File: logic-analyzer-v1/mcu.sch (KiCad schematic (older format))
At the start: 18 parts

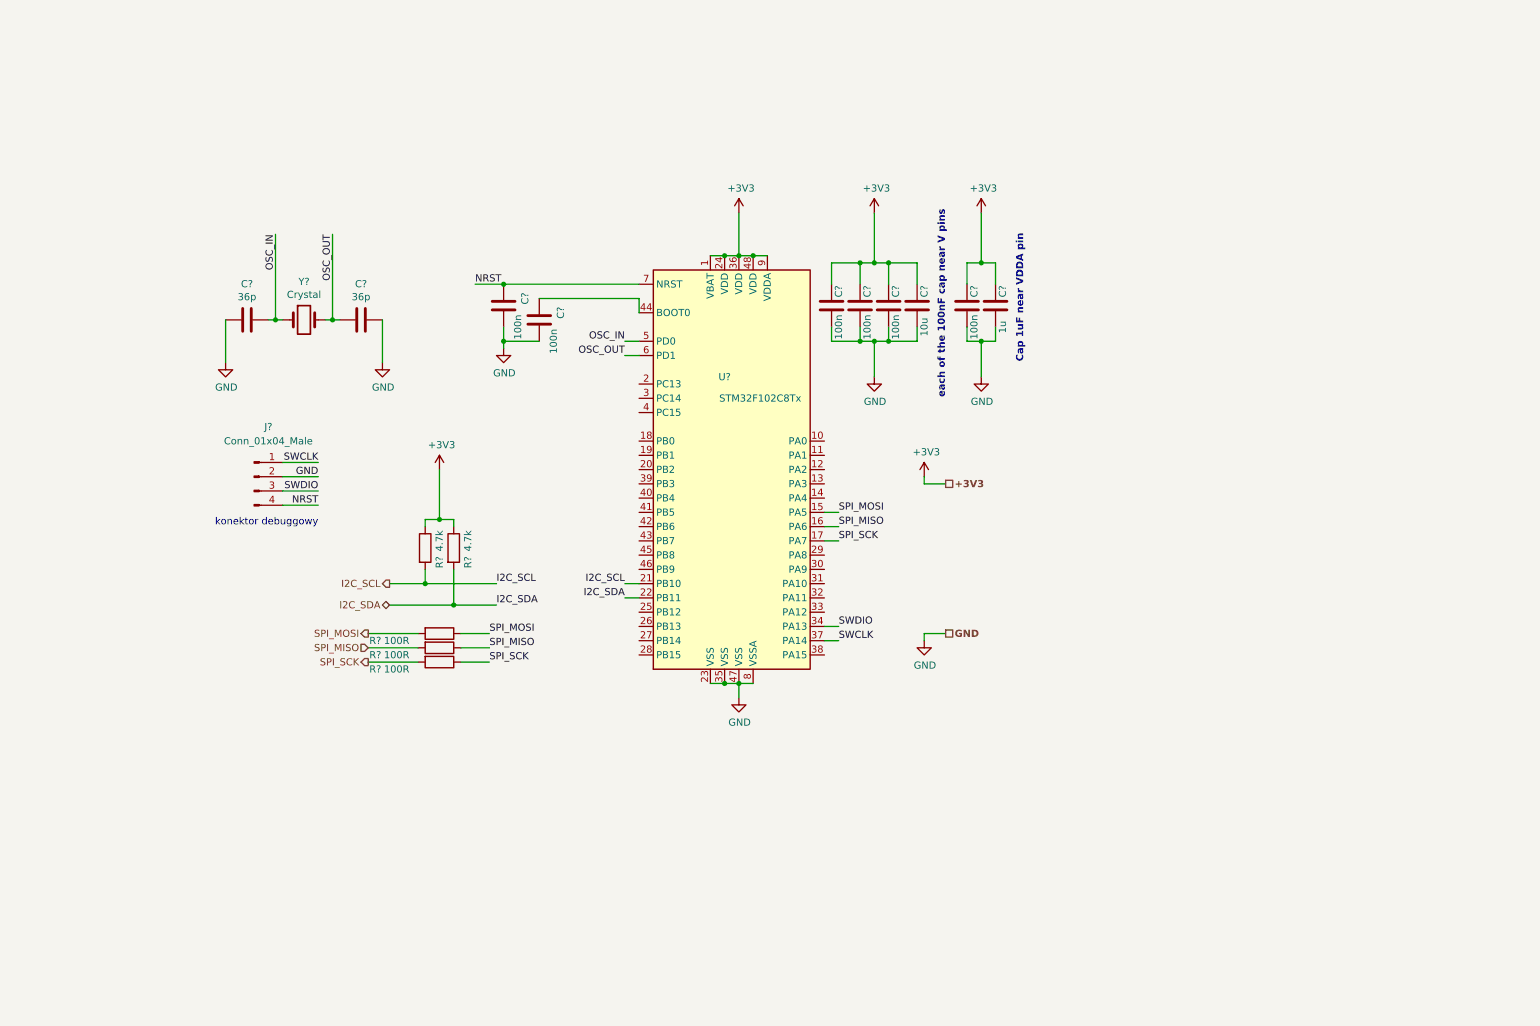
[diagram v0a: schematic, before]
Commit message: MOD usb power nets fix, mcu fixes
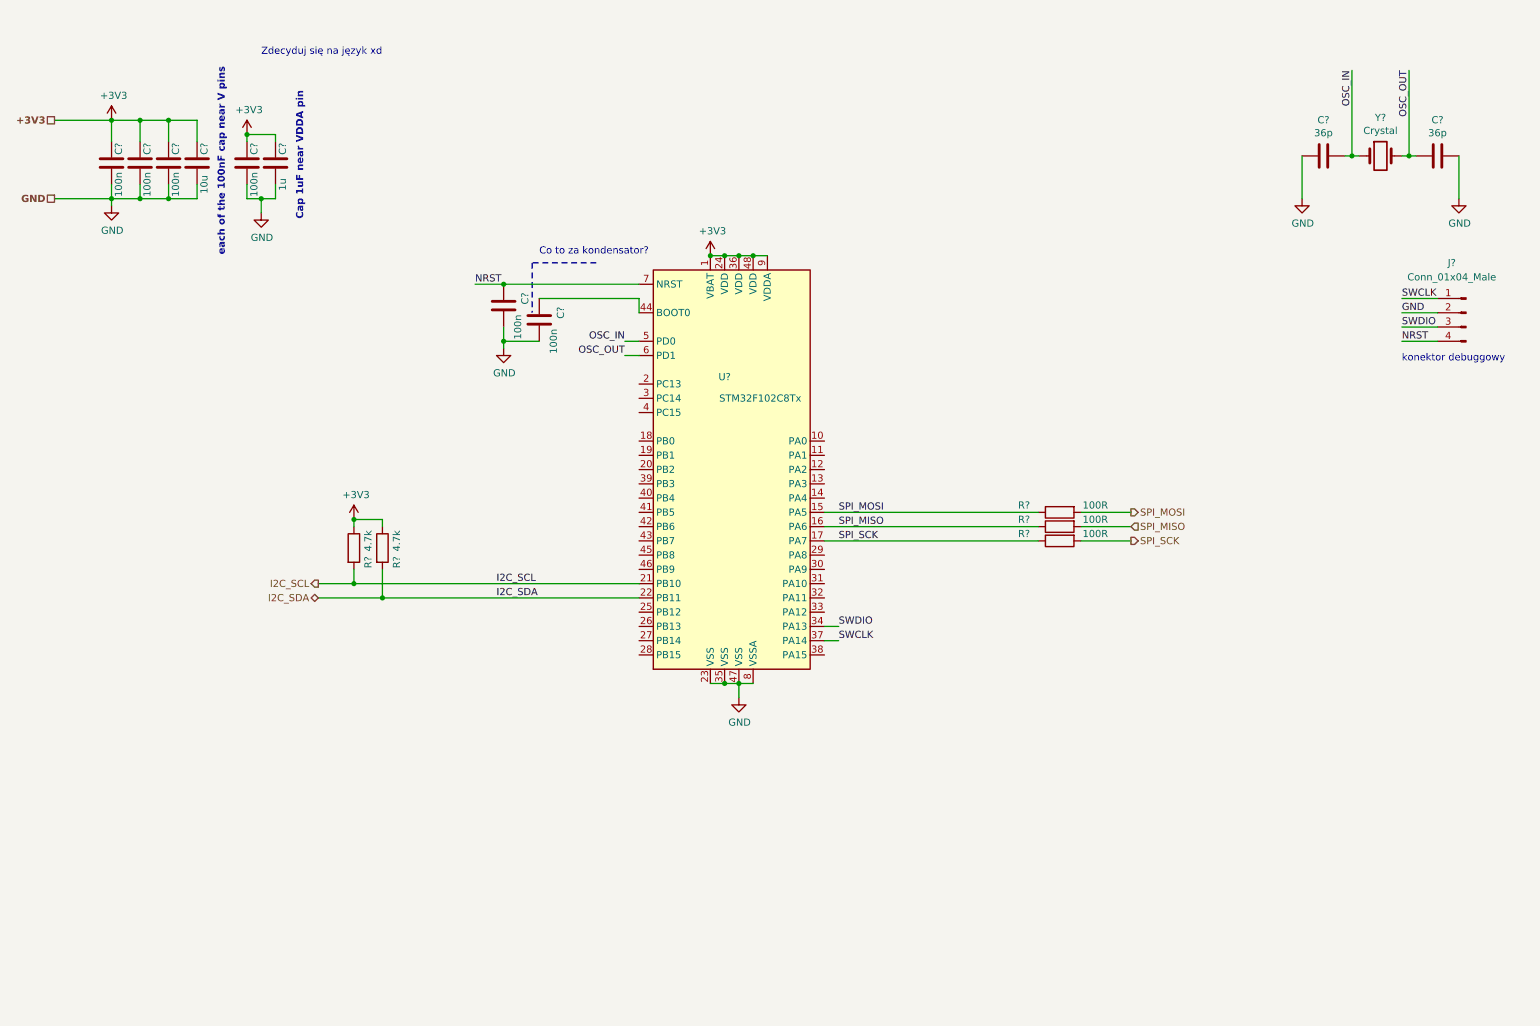
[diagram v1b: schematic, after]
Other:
- note added: "Co to za kondensator?\n"
- note added: "Zdecyduj się na język xd"
- moved on the sheet: C?, J?, R?, Y?

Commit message: adding gpio pins, usb pins, usart pins
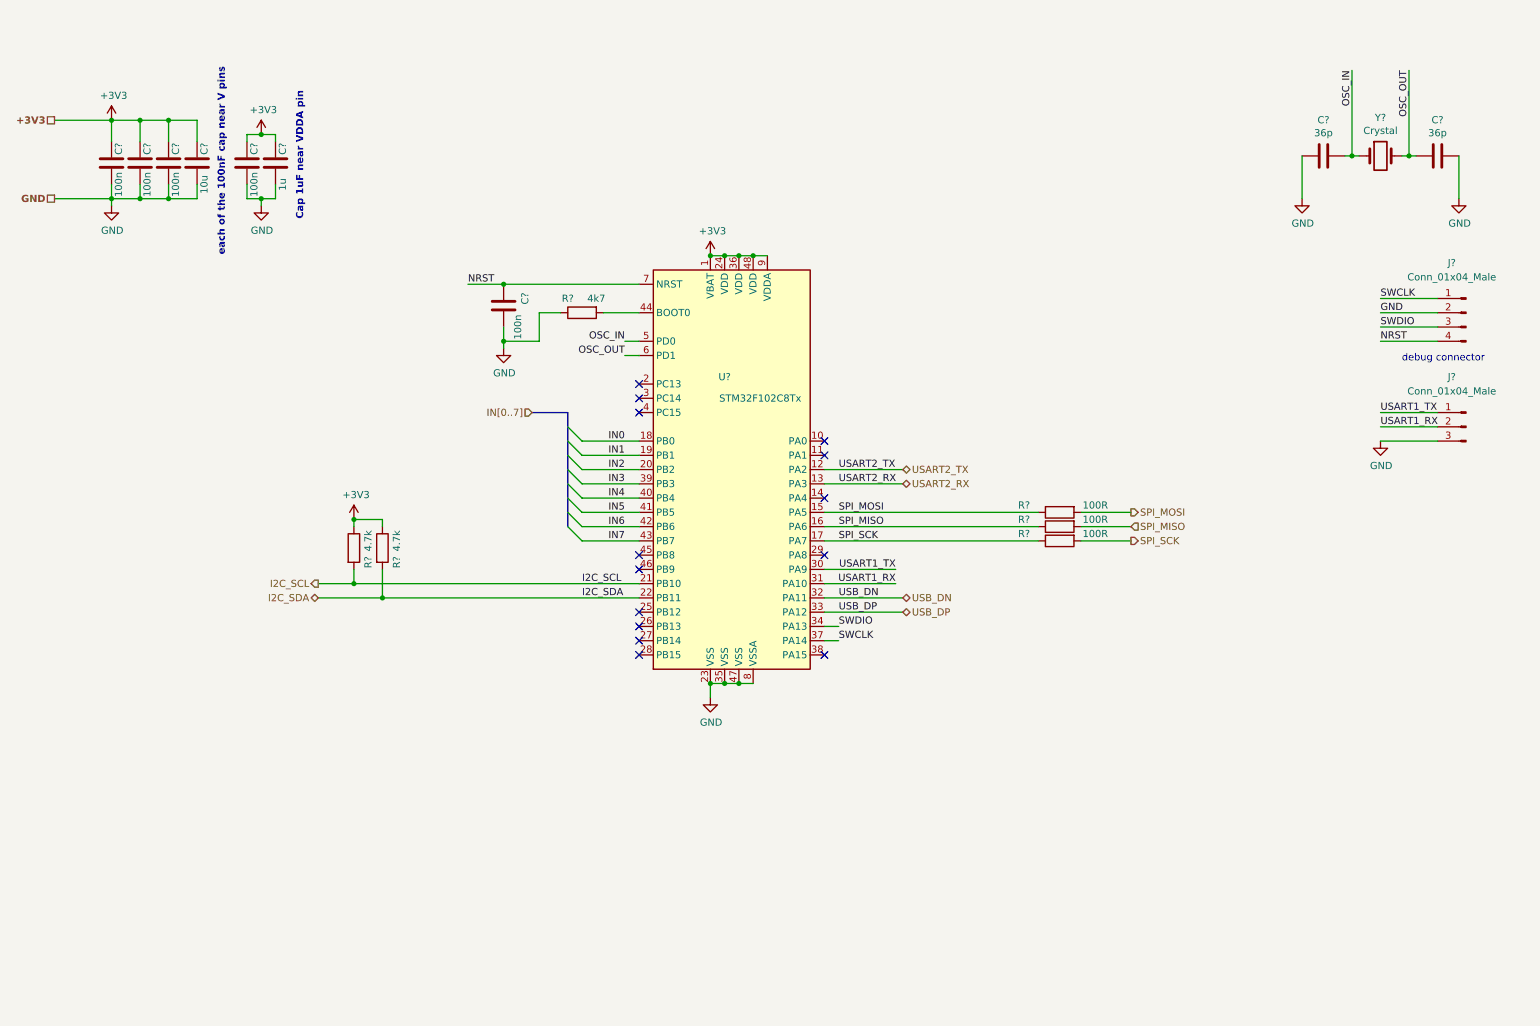
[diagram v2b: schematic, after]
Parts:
- removed C?: 100n, Capacitor_SMD:C_0603_1608Metric_Pad1.05x0.95mm_HandSolder, symbol Device:C
- added J?: Conn_01x04_Male, symbol Connector:Conn_01x03_Male
- added R?: 4k7, Resistor_SMD:R_0603_1608Metric_Pad1.05x0.95mm_HandSolder, symbol Device:R
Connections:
- net GND: now also J?.3 (Pin_3), R?.1
- net USART2_TX: now reaches U?.12 (PA2)
- net USART2_RX: now reaches U?.13 (PA3)
- net IN0: now reaches U?.18 (PB0)
- net IN1: now reaches U?.19 (PB1)
- net IN2: now reaches U?.20 (PB2)
- net USART1_TX: now reaches U?.30 (PA9)
- net USART1_TX: now also J?.1 (Pin_1)
- net USART1_RX: now reaches U?.31 (PA10)
- net USART1_RX: now also J?.2 (Pin_2)
- net USB_DN: now reaches U?.32 (PA11)
- net USB_DP: now reaches U?.33 (PA12)
- net IN3: now reaches U?.39 (PB3)
- net IN4: now reaches U?.40 (PB4)
- net IN5: now reaches U?.41 (PB5)
- net IN6: now reaches U?.42 (PB6)
- net IN7: now reaches U?.43 (PB7)
- net at U?.44 (BOOT0): now also R?.2
- no-connect marks 0 -> 14
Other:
- note added: "debug connector"
- note removed: "Co to za kondensator?\n"
- note removed: "Zdecyduj się na język xd"
- note removed: "konektor debuggowy"
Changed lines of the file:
@@
 L power:GND #PWR?
 U 1 1 5F3DC23A
-P 2250 2000
-F 0 "#PWR?" H 2250 1750 50  0001 C CNN
-F 1 "GND" H 2255 1827 50  0000 C CNN
-F 2 "" H 2250 2000 50  0001 C CNN
-F 3 "" H 2250 2000 50  0001 C CNN
-	1    2250 2000
-	1    0    0    -1
-$EndComp
-Wire Wire Line
-	2250 2000 2250 1900
+P 2250 1950
+F 0 "#PWR?" H 2250 1700 50  0001 C CNN
+F 1 "GND" H 2255 1777 50  0000 C CNN
+F 2 "" H 2250 1950 50  0001 C CNN
+F 3 "" H 2250 1950 50  0001 C CNN
+	1    2250 1950
+	1    0    0    -1
+$EndComp
+Wire Wire Line
+	2250 1950 2250 1900
 $Comp
 L power:GND #PWR?
 U 1 1 5F3DDEC8
-P 5600 5400
-F 0 "#PWR?" H 5600 5150 50  0001 C CNN
-F 1 "GND" H 5605 5227 50  0000 C CNN
-F 2 "" H 5600 5400 50  0001 C CNN
-F 3 "" H 5600 5400 50  0001 C CNN
-	1    5600 5400
-	1    0    0    -1
-$EndComp
-Wire Wire Line
-	5600 5400 5600 5300
+P 5400 5400
+F 0 "#PWR?" H 5400 5150 50  0001 C CNN
+F 1 "GND" H 5405 5227 50  0000 C CNN
+F 2 "" H 5400 5400 50  0001 C CNN
+F 3 "" H 5400 5400 50  0001 C CNN
+	1    5400 5400
+	1    0    0    -1
+$EndComp
 Text Notes 2550 2050 1    50   ~ 10
 Cap 1uF near VDDA pin
@@
 	3100 4500 3100 4700
 Connection ~ 3100 4700
-Text Label 3900 4600 0    50   ~ 0
+Text Label 4500 4600 0    50   ~ 0
 I2C_SCL
-Text Label 3900 4700 0    50   ~ 0
+Text Label 4500 4700 0    50   ~ 0
 I2C_SDA
 Text HLabel 2650 4600 0    50   Output ~ 0
@@
 	2900 4150 2900 4200
 Text Notes 10250 3050 0    50   ~ 0
-konektor debuggowy
-Text Label 10250 2700 0    50   ~ 0
+debug connector
+Text Label 10100 2700 0    50   ~ 0
 GND
-Text Label 10250 2600 0    50   ~ 0
+Text Label 10100 2600 0    50   ~ 0
 SWCLK
-Text Label 10250 2800 0    50   ~ 0
+Text Label 10100 2800 0    50   ~ 0
 SWDIO
-Text Label 10250 2900 0    50   ~ 0
+Text Label 10100 2900 0    50   ~ 0
 NRST
 Wire Wire Line
@@
 	1    0    0    -1
 $EndComp
-Text Label 3750 2500 0    50   ~ 0
+Text Label 3700 2500 0    50   ~ 0
 NRST
 Wire Wire Line
-	3950 2500 3750 2500
+	3950 2500 3700 2500
 Connection ~ 3950 2500
 Text HLabel 800  1900 0    50   UnSpc ~ 10
@@
 	3950 2500 4900 2500
 Wire Wire Line
-	4900 2700 4900 2600
-$Comp
-L Device:C C?
-U 1 1 5F508F55
-P 4200 2750
-F 0 "C?" V 4050 2700 50  0000 C CNN
-F 1 "100n" V 4100 2900 50  0000 C CNN
-F 2 "Capacitor_SMD:C_0603_1608Metric_Pad1.05x0.95mm_HandSolder" H 4238 2600 50  0001 C CNN
-F 3 "~" H 4200 2750 50  0001 C CNN
-	1    4200 2750
-	-1   0    0    1
-$EndComp
-Wire Wire Line
 	4200 2900 3950 2900
 Wire Wire Line
@@
 	3950 2800 3950 2900
 Connection ~ 3950 2900
-Wire Wire Line
-	4200 2600 4900 2600
 $Comp
 L power:+3V3 #PWR?
@@
 L power:+3V3 #PWR?
 U 1 1 5F526039
-P 2150 1450
-F 0 "#PWR?" H 2150 1300 50  0001 C CNN
-F 1 "+3V3" H 2165 1623 50  0000 C CNN
-F 2 "" H 2150 1450 50  0001 C CNN
-F 3 "" H 2150 1450 50  0001 C CNN
-	1    2150 1450
+P 2250 1450
+F 0 "#PWR?" H 2250 1300 50  0001 C CNN
+F 1 "+3V3" H 2265 1623 50  0000 C CNN
+F 2 "" H 2250 1450 50  0001 C CNN
+F 3 "" H 2250 1450 50  0001 C CNN
+	1    2250 1450
 	1    0    0    -1
 $EndComp
@@
 $EndComp
 Wire Wire Line
-	10500 2600 10250 2600
-Wire Wire Line
-	10500 2700 10250 2700
-Wire Wire Line
-	10500 2800 10250 2800
-Wire Wire Line
-	10500 2900 10250 2900
+	10500 2600 10100 2600
+Wire Wire Line
+	10500 2700 10100 2700
+Wire Wire Line
+	10500 2800 10100 2800
+Wire Wire Line
+	10500 2900 10100 2900
 Wire Wire Line
 	3100 4150 2900 4150
@@
 	1400 1350 1600 1350
 Wire Wire Line
-	2350 1450 2150 1450
-Connection ~ 2150 1450
+	2350 1450 2250 1450
 Wire Wire Line
 	2350 1500 2350 1450
@@
 Wire Wire Line
 	6200 4300 7700 4300
-Text Notes 4200 2300 0    50   ~ 0
-Co to za kondensator?\n
 Wire Wire Line
 	2900 4600 4900 4600
 Wire Wire Line
 	3100 4700 4900 4700
-Text Notes 2250 900  0    50   ~ 0
-Zdecyduj się na język xd
-Wire Notes Line
-	4600 2350 4150 2350
-Wire Notes Line
-	4150 2350 4150 2700
+$Comp
+L Device:R R?
+U 1 1 5F415484
+P 4500 2700
+AR Path="/5F08ED8D/5F415484" Ref="R?"  Part="1"
+AR Path="/5F19654C/5F415484" Ref="R?"  Part="1"
+F 0 "R?" V 4400 2800 50  0000 C CNN
+F 1 "4k7" V 4400 2600 50  0000 C CNN
+F 2 "Resistor_SMD:R_0603_1608Metric_Pad1.05x0.95mm_HandSolder" V 4430 2700 50  0001 C CNN
+F 3 "~" H 4500 2700 50  0001 C CNN
+	1    4500 2700
+	0    -1   1    0
+$EndComp
+Wire Wire Line
+	4200 2900 4200 2700
+Wire Wire Line
+	4200 2700 4350 2700
+Wire Wire Line
+	4650 2700 4900 2700
+Connection ~ 2250 1450
+Wire Wire Line
+	2250 1450 2150 1450
+Wire Wire Line
+	5400 5400 5400 5300
+Connection ~ 5400 5300
+Wire Wire Line
+	6750 4700 6200 4700
+Wire Wire Line
+	6750 4800 6200 4800
+Text Label 6300 4700 0    50   ~ 0
+USB_DN
+Text Label 6300 4800 0    50   ~ 0
+USB_DP
+Wire Wire Line
+	6700 4500 6200 4500
+Wire Wire Line
+	6700 4600 6200 4600
+Text Label 6700 4500 2    50   ~ 0
+USART1_TX
+Text Label 6700 4600 2    50   ~ 0
+USART1_RX
+Wire Wire Line
+	6750 3800 6200 3800
+Wire Wire Line
+	6750 3900 6200 3900
+Text Label 6300 3800 0    50   ~ 0
+USART2_TX
+Text Label 6300 3900 0    50   ~ 0
+USART2_RX
+Entry Wire Line
+	4500 4300 4400 4200
+Entry Wire Line
+	4500 4200 4400 4100
+Entry Wire Line
+	4500 4100 4400 4000
+Entry Wire Line
+	4500 4000 4400 3900
+Entry Wire Line
+	4500 3900 4400 3800
+Entry Wire Line
+	4500 3800 4400 3700
+Entry Wire Line
+	4500 3700 4400 3600
+Entry Wire Line
+	4500 3600 4400 3500
+Text HLabel 4150 3400 0    50   Input ~ 0
+IN[0..7]
+Text Label 4800 3600 2    50   ~ 0
+IN0
+Text Label 4800 3700 2    50   ~ 0
+IN1
+Text Label 4800 3800 2    50   ~ 0
+IN2
+Text Label 4800 3900 2    50   ~ 0
+IN3
+Text Label 4800 4000 2    50   ~ 0
+IN4
+Text Label 4800 4100 2    50   ~ 0
+IN5
+Text Label 4800 4200 2    50   ~ 0
+IN6
+Text Label 4800 4300 2    50   ~ 0
+IN7
+Wire Wire Line
+	4500 4300 4900 4300
+Wire Wire Line
+	4500 4200 4900 4200
+Wire Wire Line
+	4500 4100 4900 4100
+Wire Wire Line
+	4500 4000 4900 4000
+Wire Wire Line
+	4500 3900 4900 3900
+Wire Wire Line
+	4500 3800 4900 3800
+Wire Wire Line
+	4500 3700 4900 3700
+Wire Wire Line
+	4500 3600 4900 3600
+NoConn ~ 4900 3200
+NoConn ~ 4900 3300
+NoConn ~ 4900 3400
+NoConn ~ 4900 4400
+NoConn ~ 4900 4500
+NoConn ~ 4900 4800
+NoConn ~ 4900 4900
+NoConn ~ 4900 5000
+NoConn ~ 4900 5100
+NoConn ~ 6200 3600
+NoConn ~ 6200 3700
+NoConn ~ 6200 4000
+NoConn ~ 6200 4400
+NoConn ~ 6200 5100
+Text HLabel 6750 4700 2    50   BiDi ~ 0
+USB_DN
+Text HLabel 6750 4800 2    50   BiDi ~ 0
+USB_DP
+Text HLabel 6750 3800 2    50   BiDi ~ 0
+USART2_TX
+Text HLabel 6750 3900 2    50   BiDi ~ 0
+USART2_RX
+Wire Bus Line
+	4150 3400 4400 3400
+$Comp
+L Connector:Conn_01x03_Male J?
+U 1 1 5F5072CB
+P 10700 3500
+F 0 "J?" H 10800 3850 50  0000 C CNN
+F 1 "Conn_01x04_Male" H 10800 3750 50  0000 C CNN
+F 2 "" H 10700 3500 50  0001 C CNN
+F 3 "~" H 10700 3500 50  0001 C CNN
+	1    10700 3500
+	-1   0    0    -1
+$EndComp
+Wire Wire Line
+	10500 3400 10100 3400
+Wire Wire Line
+	10500 3500 10100 3500
+Wire Wire Line
+	10500 3600 10100 3600
+$Comp
+L power:GND #PWR?
+U 1 1 5F515523
+P 10100 3600
+F 0 "#PWR?" H 10100 3350 50  0001 C CNN
+F 1 "GND" H 10105 3427 50  0000 C CNN
+F 2 "" H 10100 3600 50  0001 C CNN
+F 3 "" H 10100 3600 50  0001 C CNN
+	1    10100 3600
+	1    0    0    -1
+$EndComp
+Text Label 10100 3400 0    50   ~ 0
+USART1_TX
+Text Label 10100 3500 0    50   ~ 0
+USART1_RX
+Wire Bus Line
+	4400 3400 4400 4200
 $EndSCHEMATC
